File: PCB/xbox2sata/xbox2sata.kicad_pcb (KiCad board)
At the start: 4 copper layers, 156 x 90 mm, 3 parts, among them J1 61203921621, J2 67800-8025, U1 88SA8052

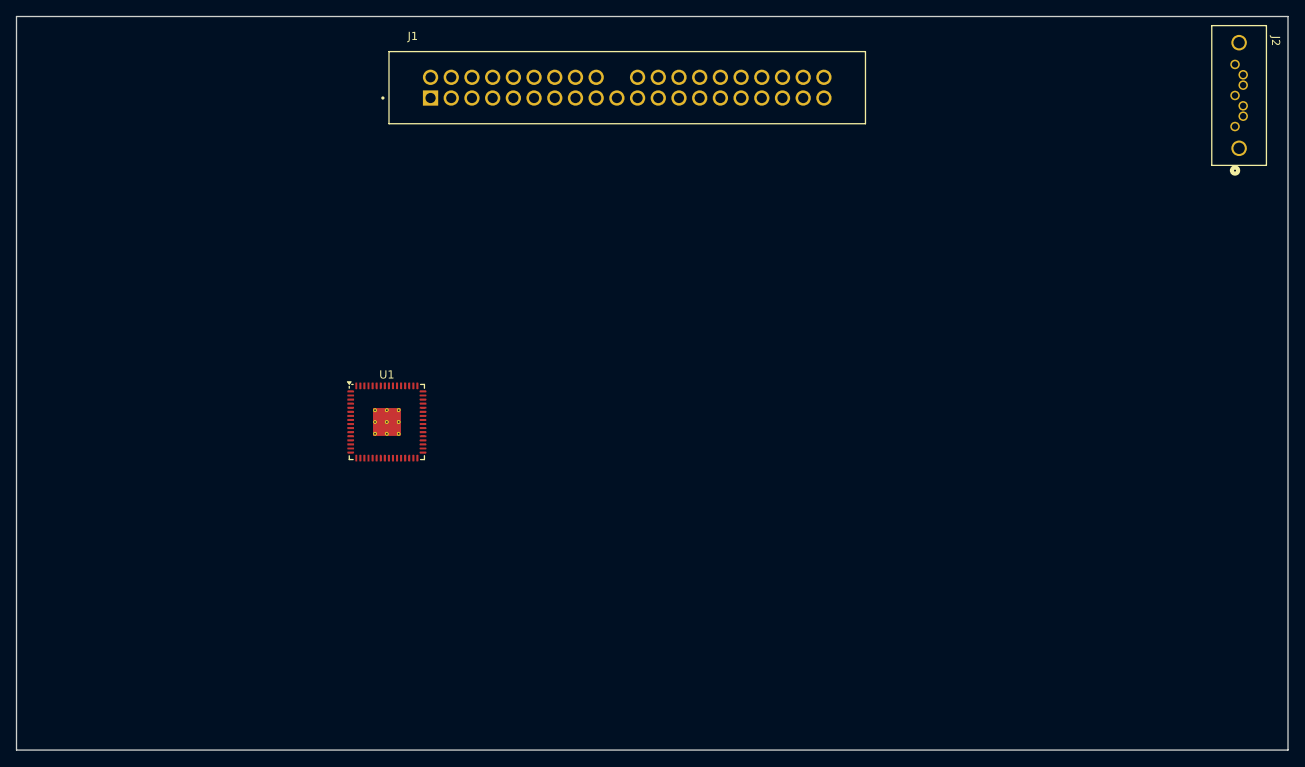
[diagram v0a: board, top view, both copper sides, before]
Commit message: KiCad updates
Crystal resonator added, 3d model for ide header fixed.
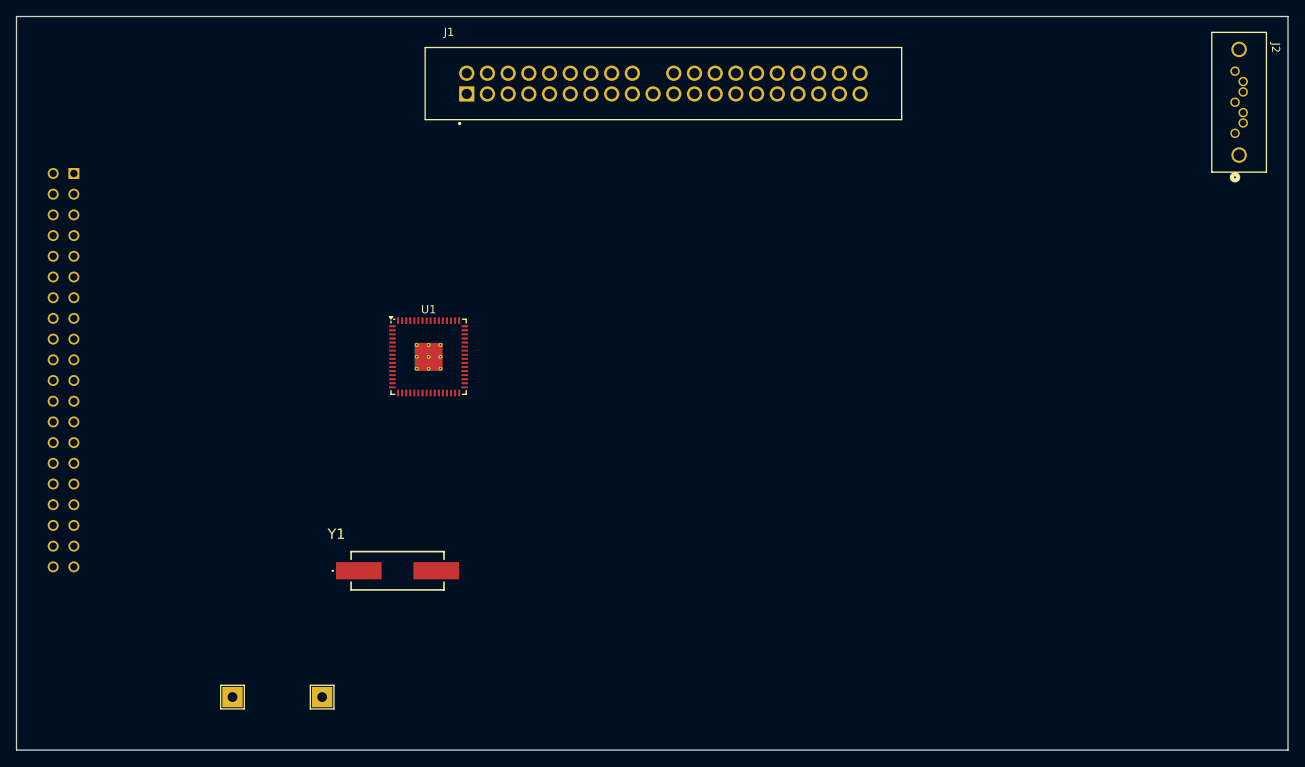
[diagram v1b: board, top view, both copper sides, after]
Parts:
- added J3: 90151-2140, xbox2sata:RHDR40W70P254_2X20_5065X498X870P, B.Cu at (95.5, 82.8)
- added TP1: xbox_ground, TestPoint:TestPoint_THTPad_2.5x2.5mm_Drill1.2mm, F.Cu at (126.0, 147.0)
- added TP2: xbox_3V3, TestPoint:TestPoint_THTPad_2.5x2.5mm_Drill1.2mm, F.Cu at (115.0, 147.0)
- added Y1: ABLS-25.000MHZ-B4-F-T, xbox2sata:Crystal, F.Cu at (135.2, 131.5)
- moved U1 9.50 mm to (139.1, 105.2)
- moved J1 4.47 mm to (167.9, 71.7)
- moved J2 0.83 mm to (238.0, 77.8)
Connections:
- J2 pad 8: (no net) -> unconnected-(J2-mount_1-Pad8)
- J2 pad 9: (no net) -> unconnected-(J2-mount_2-Pad9)
- U1 pad 65: (no net) -> unconnected-(U1-GND-Pad65)
